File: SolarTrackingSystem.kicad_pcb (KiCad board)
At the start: 2 copper layers, 57 x 54 mm, 8 parts, among them J1 Servo Pin Connector, J2 LDR Terminal, J3 LDR Terminal (1)

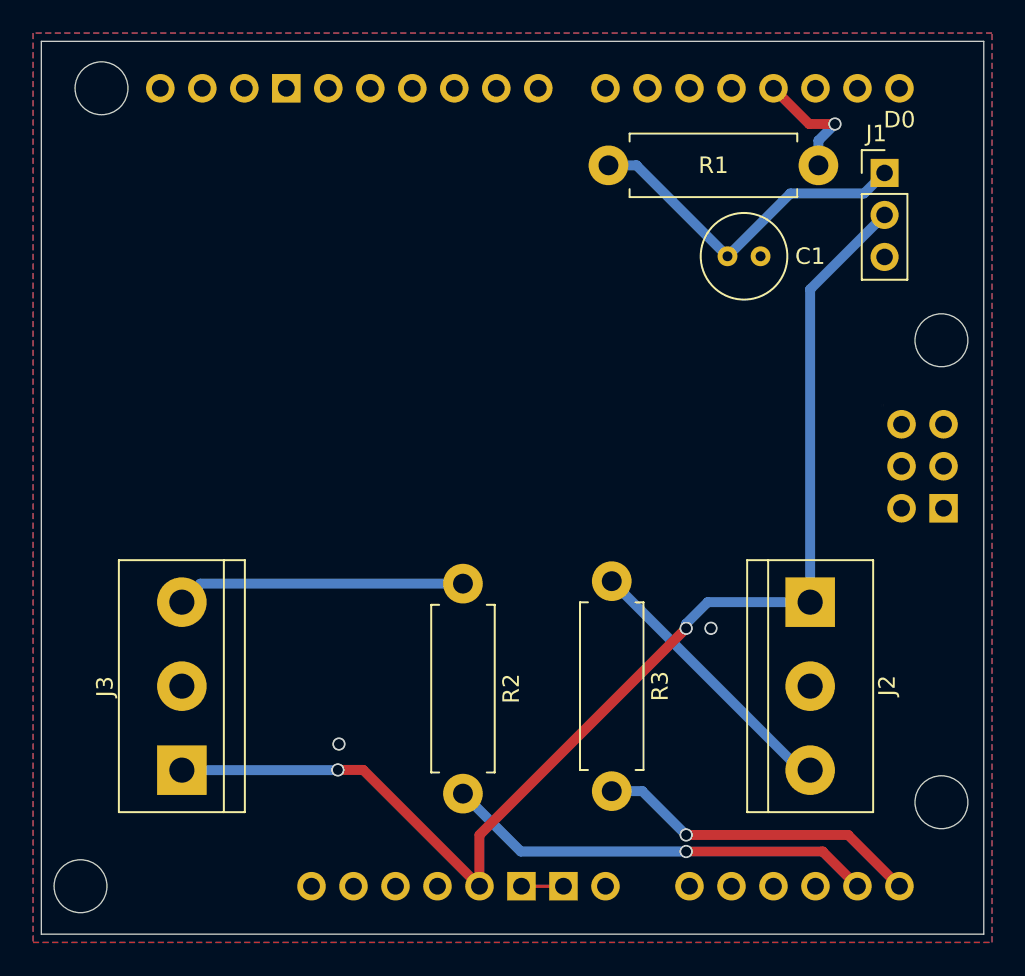
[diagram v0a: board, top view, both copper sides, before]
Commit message: version 3
made tracks thicker
removed vias
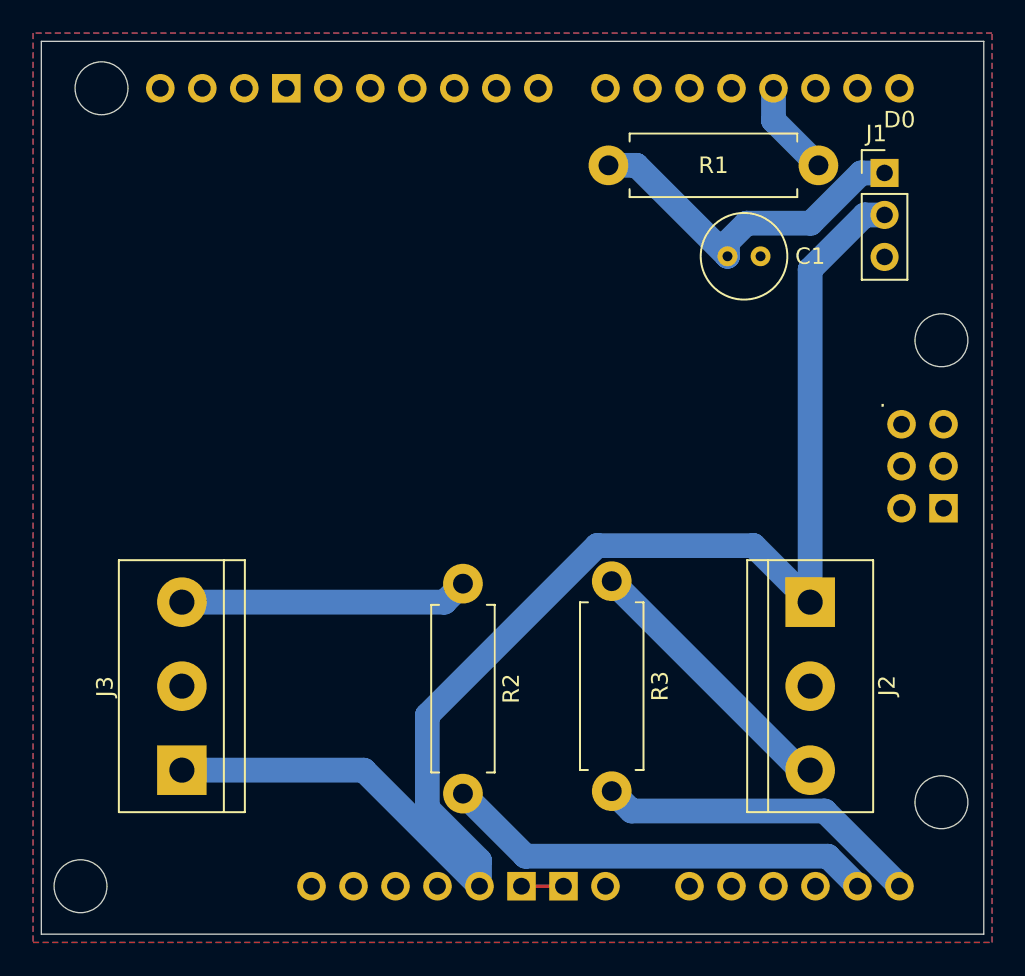
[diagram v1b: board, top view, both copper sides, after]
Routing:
- net /5V_pin: track 75.3 -> 87.4 mm, vias 2 -> 0
- net Net-(A1-D3_INT1): track 7.53 -> 5.79 mm, vias 1 -> 0
- net Net-(A1-PadA5): vias 1 -> 0
- net Net-(A1-PadA4): vias 1 -> 0
- net GND: vias 2 -> 0
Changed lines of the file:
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@@
-			)
-		)
-		(fp_text user "."
-			(at 62.484 -32.004 0)
-			(layer "F.SilkS")
-			(effects
-				(font
-					(size 1 1)
-					(thickness 0.15)
-				)
-				(justify mirror)
 			)
 		)
@@
 				)
 				(justify mirror)
+			)
+		)
+		(fp_text user "."
+			(at 62.484 -32.004 -0)
+			(layer "B.SilkS")
+			(effects
+				(font
+					(size 1 1)
+					(thickness 0.15)
+				)
 			)
 		)
@@
 	)
 	(segment
-		(start 158.5 63.5)
-		(end 156.94 63.5)
-		(width 0.6)
-		(layer "F.Cu")
+		(start 154.78 63.28)
+		(end 154.78 61.34)
+		(width 1.5)
+		(layer "B.Cu")
 		(net 4)
 	)
 	(segment
-		(start 156.94 63.5)
-		(end 154.78 61.34)
-		(width 0.6)
-		(layer "F.Cu")
-		(net 4)
-	)
-	(via
-		(at 158.5 63.5)
-		(size 0.8)
-		(drill 0.6)
-		(layers "F.Cu" "B.Cu")
-		(net 4)
-	)
-	(segment
 		(start 157.5 66)
-		(end 157.5 64.5)
-		(width 0.6)
-		(layer "B.Cu")
-		(net 4)
-	)
-	(segment
-		(start 157.5 64.5)
-		(end 158.5 63.5)
-		(width 0.6)
+		(end 154.78 63.28)
+		(width 1.5)
 		(layer "B.Cu")
 		(net 4)
@@
 		(net 12)
 	)
-	(via
-		(at 128.5 101)
-		(size 0.8)
-		(drill 0.6)
-		(layers "F.Cu" "B.Cu")
-		(net 12)
-	)
-	(via
-		(at 151 94)
-		(size 0.8)
-		(drill 0.6)
-		(layers "F.Cu" "B.Cu")
-		(net 12)
-	)
 	(segment
 		(start 154.04 71.54)
@@
 	)
 	(segment
-		(start 149.5 107.5)
-		(end 157.76 107.5)
-		(width 0.6)
-		(layer "F.Cu")
+		(start 159.86 109.573768)
+		(end 159.86 109.6)
+		(width 1.5)
+		(layer "B.Cu")
 		(net 14)
 	)
 	(segment
-		(start 157.76 107.5)
-		(end 159.86 109.6)
-		(width 0.6)
-		(layer "F.Cu")
+		(start 136 104)
+		(end 139.7854 107.7854)
+		(width 1.5)
+		(layer "B.Cu")
 		(net 14)
 	)
-	(via
-		(at 149.5 107.5)
-		(size 0.8)
-		(drill 0.6)
-		(layers "F.Cu" "B.Cu")
+	(segment
+		(start 158.071632 107.7854)
+		(end 159.86 109.573768)
+		(width 1.5)
+		(layer "B.Cu")
 		(net 14)
 	)
 	(segment
-		(start 139.5 107.5)
-		(end 149.5 107.5)
-		(width 0.6)
+		(start 139.7854 107.7854)
+		(end 158.071632 107.7854)
+		(width 1.5)
 		(layer "B.Cu")
 		(net 14)
 	)
 	(segment
-		(start 136 104)
-		(end 139.5 107.5)
-		(width 0.6)
-		(layer "B.Cu")
-		(net 14)
-	)
-	(segment
 		(start 137 109.6)
-		(end 137 106.5)
-		(width 0.6)
-		(layer "F.Cu")
+		(end 137 108.041974)
+		(width 1.5)
+		(layer "B.Cu")
 		(net 17)
 	)
 	(segment
-		(start 128.434314 102.565686)
-		(end 129.965686 102.565686)
-		(width 0.6)
-		(layer "F.Cu")
+		(start 133.849 104.890974)
+		(end 133.849 99.259026)
+		(width 1.5)
+		(layer "B.Cu")
 		(net 17)
 	)
 	(segment
-		(start 137 106.5)
-		(end 149.5 94)
-		(width 0.6)
-		(layer "F.Cu")
+		(start 130.006232 102.58)
+		(end 137 109.573768)
+		(width 1.5)
+		(layer "B.Cu")
 		(net 17)
 	)
 	(segment
-		(start 129.965686 102.565686)
+		(start 153.579 88.999)
+		(end 157 92.42)
+		(width 1.5)
+		(layer "B.Cu")
+		(net 17)
+	)
+	(segment
+		(start 160.297919 69)
+		(end 157 72.297919)
+		(width 1.5)
+		(layer "B.Cu")
+		(net 17)
+	)
+	(segment
+		(start 137 108.041974)
+		(end 133.849 104.890974)
+		(width 1.5)
+		(layer "B.Cu")
+		(net 17)
+	)
+	(segment
+		(start 157 72.297919)
+		(end 157 92.42)
+		(width 1.5)
+		(layer "B.Cu")
+		(net 17)
+	)
+	(segment
+		(start 144.109026 88.999)
+		(end 153.579 88.999)
+		(width 1.5)
+		(layer "B.Cu")
+		(net 17)
+	)
+	(segment
+		(start 133.849 99.259026)
+		(end 144.109026 88.999)
+		(width 1.5)
+		(layer "B.Cu")
+		(net 17)
+	)
+	(segment
+		(start 161.5 69)
+		(end 160.297919 69)
+		(width 1.5)
+		(layer "B.Cu")
+		(net 17)
+	)
+	(segment
+		(start 119 102.58)
+		(end 130.006232 102.58)
+		(width 1.5)
+		(layer "B.Cu")
+		(net 17)
+	)
+	(segment
+		(start 137 109.573768)
 		(end 137 109.6)
-		(width 0.6)
-		(layer "F.Cu")
+		(width 1.5)
+		(layer "B.Cu")
 		(net 17)
 	)
-	(via
-		(at 149.5 94)
-		(size 0.8)
-		(drill 0.6)
-		(layers "F.Cu" "B.Cu")
-		(net 17)
-	)
-	(via
-		(at 128.434314 102.565686)
-		(size 0.8)
-		(drill 0.6)
-		(layers "F.Cu" "B.Cu")
-		(net 17)
-	)
-	(segment
-		(start 128.42 102.58)
-		(end 128.434314 102.565686)
-		(width 0.6)
-		(layer "B.Cu")
-		(net 17)
-	)
-	(segment
-		(start 157 92.42)
-		(end 150.805793 92.42)
-		(width 0.6)
-		(layer "B.Cu")
-		(net 17)
-	)
-	(segment
-		(start 149.5 93.725793)
-		(end 149.5 94)
-		(width 0.6)
-		(layer "B.Cu")
-		(net 17)
-	)
-	(segment
-		(start 157 73.5)
-		(end 157 92.42)
-		(width 0.6)
-		(layer "B.Cu")
-		(net 17)
-	)
-	(segment
-		(start 150.805793 92.42)
-		(end 149.5 93.725793)
-		(width 0.6)
-		(layer "B.Cu")
-		(net 17)
-	)
-	(segment
-		(start 119 102.58)
-		(end 128.42 102.58)
-		(width 0.6)
-		(layer "B.Cu")
-		(net 17)
-	)
-	(segment
-		(start 161.5 69)
-		(end 157 73.5)
-		(width 0.6)
-		(layer "B.Cu")
-		(net 17)
-	)
-	(segment
-		(start 159.3 106.5)
+	(segment
+		(start 162.4 109.573768)
 		(end 162.4 109.6)
-		(width 0.6)
-		(layer "F.Cu")
+		(width 1.5)
+		(layer "B.Cu")
 		(net 29)
 	)
 	(segment
-		(start 149.5 106.5)
-		(end 159.3 106.5)
-		(width 0.6)
-		(layer "F.Cu")
+		(start 146.2 105.05)
+		(end 157.876232 105.05)
+		(width 1.5)
+		(layer "B.Cu")
 		(net 29)
 	)
-	(via
-		(at 149.5 106.5)
-		(size 0.8)
-		(drill 0.6)
-		(layers "F.Cu" "B.Cu")
+	(segment
+		(start 157.876232 105.05)
+		(end 162.4 109.573768)
+		(width 1.5)
+		(layer "B.Cu")
 		(net 29)
 	)
 	(segment
 		(start 145 103.85)
-		(end 146.85 103.85)
-		(width 0.6)
+		(end 146.2 105.05)
+		(width 1.5)
 		(layer "B.Cu")
 		(net 29)
 	)
 	(segment
-		(start 146.85 103.85)
-		(end 149.5 106.5)
-		(width 0.6)
-		(layer "B.Cu")
-		(net 29)
+		(start 146.5 66)
+		(end 152 71.5)
+		(width 1.5)
+		(layer "B.Cu")
+		(net 37)
+	)
+	(segment
+		(start 160.081974 66.46)
+		(end 157.041974 69.5)
+		(width 1.5)
+		(layer "B.Cu")
+		(net 37)
+	)
+	(segment
+		(start 161.5 66.46)
+		(end 160.081974 66.46)
+		(width 1.5)
+		(layer "B.Cu")
+		(net 37)
+	)
+	(segment
+		(start 153.151472 69.5)
+		(end 152 70.651472)
+		(width 1.5)
+		(layer "B.Cu")
+		(net 37)
 	)
 	(segment
 		(start 144.8 66)
 		(end 146.5 66)
-		(width 0.6)
+		(width 1.5)
 		(layer "B.Cu")
 		(net 37)
 	)
 	(segment
-		(start 160.259 67.701)
-		(end 155.799 67.701)
-		(width 0.6)
+		(start 152 70.651472)
+		(end 152 71.5)
+		(width 1.5)
 		(layer "B.Cu")
 		(net 37)
 	)
 	(segment
-		(start 146.5 66)
-		(end 152 71.5)
-		(width 0.6)
+		(start 157.041974 69.5)
+		(end 153.151472 69.5)
+		(width 1.5)
 		(layer "B.Cu")
 		(net 37)
 	)
 	(segment
-		(start 155.799 67.701)
-		(end 152 71.5)
-		(width 0.6)
-		(layer "B.Cu")
-		(net 37)
-	)
-	(segment
-		(start 161.5 66.46)
-		(end 160.259 67.701)
-		(width 0.6)
-		(layer "B.Cu")
-		(net 37)
-	)
-	(segment
 		(start 156.43 102.58)
-		(end 145 91.15)
-		(width 0.6)
+		(end 157 102.58)
+		(width 1.5)
 		(layer "B.Cu")
 		(net 38)
 	)
 	(segment
-		(start 157 102.58)
+		(start 145 91.15)
 		(end 156.43 102.58)
-		(width 0.6)
+		(width 1.5)
 		(layer "B.Cu")
 		(net 38)
 	)
 	(segment
-		(start 136 91.3)
-		(end 120.12 91.3)
-		(width 0.6)
+		(start 134.88 92.42)
+		(end 136 91.3)
+		(width 1.5)
 		(layer "B.Cu")
 		(net 39)
 	)
 	(segment
-		(start 120.12 91.3)
-		(end 119 92.42)
-		(width 0.6)
+		(start 119 92.42)
+		(end 134.88 92.42)
+		(width 1.5)
 		(layer "B.Cu")
 		(net 39)
